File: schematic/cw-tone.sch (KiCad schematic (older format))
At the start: 20 parts, among them Q16 2N7000, Q17 2N7000, U10 NE5532

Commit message: Some minor tweaks
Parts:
- removed R62: 8.2K, symbol Device:R
- added RV6: 10K, symbol Device:R_POT_TRIM
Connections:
- net at D17.2 (A), D18.1 (K), R59.1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: now also RV6.1
- net at D17.1 (K), D18.2 (A), R55.1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: now also RV6.2, RV6.3
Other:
- note added: "Adjust to get a pure sine wave"
- moved on the sheet: C109, C112, Q17, R56, R57, R58, R60, R61

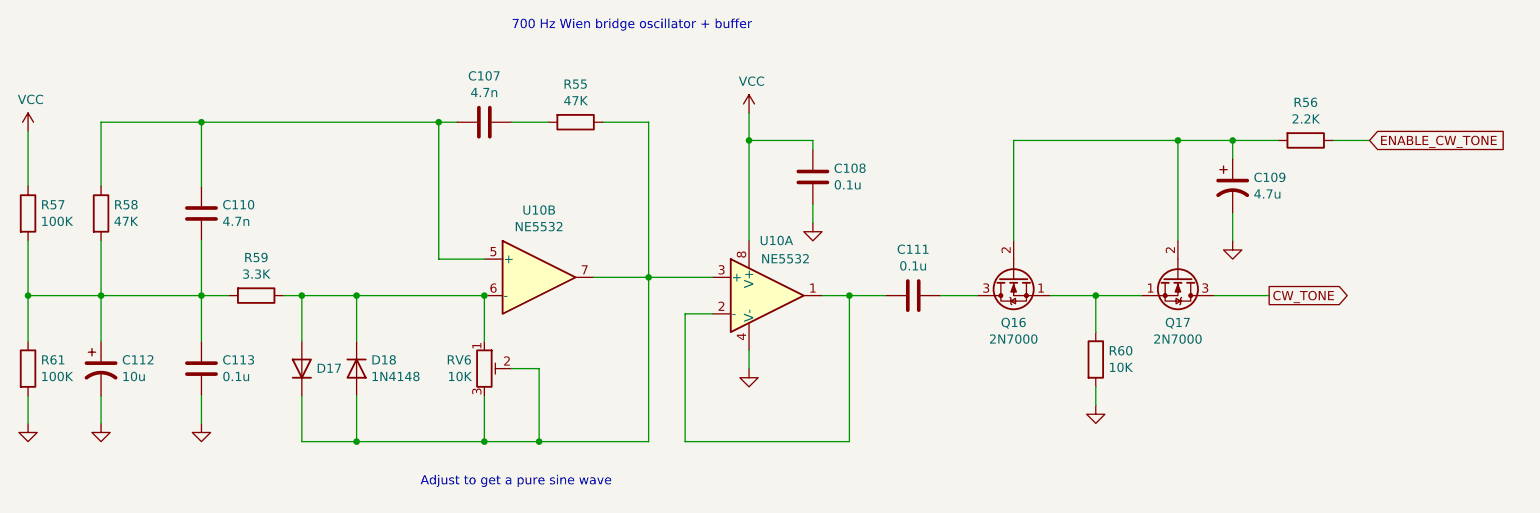
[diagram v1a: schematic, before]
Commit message: Correct the schematic
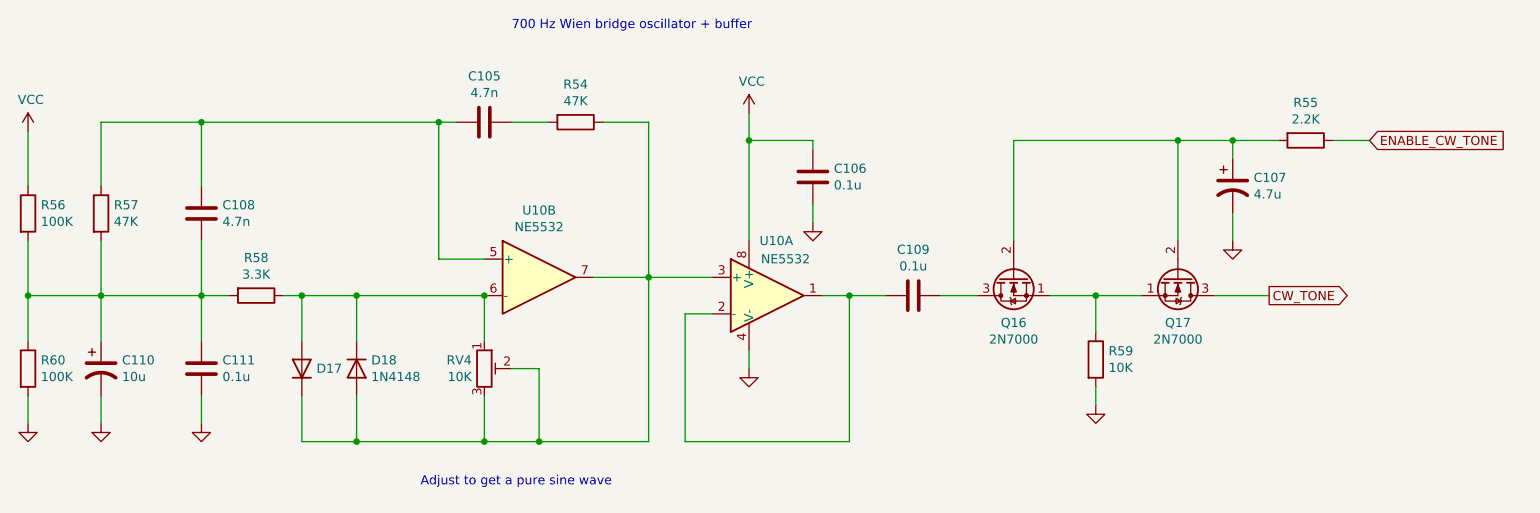
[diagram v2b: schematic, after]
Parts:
- renumbered C107 to C105, C108 to C106, C109 to C107, C110 to C108, C111 to C109, C112 to C110, C113 to C111, R55 to R54, R56 to R55, R57 to R56, R58 to R57, R59 to R58, R60 to R59, R61 to R60, RV6 to RV4
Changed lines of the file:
@@
 	5500 2450 5150 2450
 $Comp
-L power:GND #PWR0149
+L power:GND #PWR0148
 U 1 1 62E9F271
 P 5700 2950
-F 0 "#PWR0149" H 5700 2700 50  0001 C CNN
+F 0 "#PWR0148" H 5700 2700 50  0001 C CNN
 F 1 "GND" H 5705 2777 50  0001 C CNN
 F 2 "" H 5700 2950 50  0001 C CNN
@@
 	5700 2950 5700 2850
 $Comp
-L power:VCC #PWR0145
+L power:VCC #PWR0144
 U 1 1 62E9FFF5
 P 5700 1550
-F 0 "#PWR0145" H 5700 1400 50  0001 C CNN
+F 0 "#PWR0144" H 5700 1400 50  0001 C CNN
 F 1 "VCC" H 5715 1723 50  0000 C CNN
 F 2 "" H 5700 1550 50  0001 C CNN
@@
 $EndComp
 $Comp
-L Device:C C108
+L Device:C C106
 U 1 1 62EA0811
 P 6050 1900
-F 0 "C108" H 6165 1946 50  0000 L CNN
+F 0 "C106" H 6165 1946 50  0000 L CNN
 F 1 "0.1u" H 6165 1855 50  0000 L CNN
 F 2 "" H 6088 1750 50  0001 C CNN
@@
 $EndComp
 $Comp
-L power:GND #PWR0147
+L power:GND #PWR0146
 U 1 1 62EA1394
 P 6050 2150
-F 0 "#PWR0147" H 6050 1900 50  0001 C CNN
+F 0 "#PWR0146" H 6050 1900 50  0001 C CNN
 F 1 "GND" H 6055 1977 50  0001 C CNN
 F 2 "" H 6050 2150 50  0001 C CNN
@@
 Connection ~ 5700 1700
 $Comp
-L Device:C C111
+L Device:C C109
 U 1 1 62EA22EF
 P 6600 2550
-F 0 "C111" V 6348 2550 50  0000 C CNN
+F 0 "C109" V 6348 2550 50  0000 C CNN
 F 1 "0.1u" V 6439 2550 50  0000 C CNN
 F 2 "" H 6638 2400 50  0001 C CNN
@@
 Connection ~ 3550 3350
 $Comp
-L Device:R R59
+L Device:R R58
 U 1 1 62EAB701
 P 3000 2550
-F 0 "R59" V 2793 2550 50  0000 C CNN
+F 0 "R58" V 2793 2550 50  0000 C CNN
 F 1 "3.3K" V 2884 2550 50  0000 C CNN
 F 2 "" V 2930 2550 50  0001 C CNN
@@
 $EndComp
 $Comp
-L Device:C C113
+L Device:C C111
 U 1 1 62EB4018
 P 2700 2950
-F 0 "C113" H 2815 2996 50  0000 L CNN
+F 0 "C111" H 2815 2996 50  0000 L CNN
 F 1 "0.1u" H 2815 2905 50  0000 L CNN
 F 2 "" H 2738 2800 50  0001 C CNN
@@
 $EndComp
 $Comp
-L Device:CP1 C112
+L Device:CP1 C110
 U 1 1 62EB4E2D
 P 2150 2950
-F 0 "C112" H 2265 2996 50  0000 L CNN
+F 0 "C110" H 2265 2996 50  0000 L CNN
 F 1 "10u" H 2265 2905 50  0000 L CNN
 F 2 "" H 2150 2950 50  0001 C CNN
@@
 $EndComp
 $Comp
-L Device:R R61
+L Device:R R60
 U 1 1 62EB5CC9
 P 1750 2950
-F 0 "R61" H 1820 2996 50  0000 L CNN
+F 0 "R60" H 1820 2996 50  0000 L CNN
 F 1 "100K" H 1820 2905 50  0000 L CNN
 F 2 "" V 1680 2950 50  0001 C CNN
@@
 Connection ~ 3250 2550
 $Comp
-L power:GND #PWR0153
+L power:GND #PWR0152
 U 1 1 62EB7348
 P 2700 3250
-F 0 "#PWR0153" H 2700 3000 50  0001 C CNN
+F 0 "#PWR0152" H 2700 3000 50  0001 C CNN
 F 1 "GND" H 2705 3077 50  0001 C CNN
 F 2 "" H 2700 3250 50  0001 C CNN
@@
 $EndComp
 $Comp
-L power:GND #PWR0152
+L power:GND #PWR0151
 U 1 1 62EB7780
 P 2150 3250
-F 0 "#PWR0152" H 2150 3000 50  0001 C CNN
+F 0 "#PWR0151" H 2150 3000 50  0001 C CNN
 F 1 "GND" H 2155 3077 50  0001 C CNN
 F 2 "" H 2150 3250 50  0001 C CNN
@@
 $EndComp
 $Comp
-L power:GND #PWR0151
+L power:GND #PWR0150
 U 1 1 62EB79E4
 P 1750 3250
-F 0 "#PWR0151" H 1750 3000 50  0001 C CNN
+F 0 "#PWR0150" H 1750 3000 50  0001 C CNN
 F 1 "GND" H 1755 3077 50  0001 C CNN
 F 2 "" H 1750 3250 50  0001 C CNN
@@
 	2700 3100 2700 3250
 $Comp
-L Device:R R57
+L Device:R R56
 U 1 1 62EBA34E
 P 1750 2100
-F 0 "R57" H 1820 2146 50  0000 L CNN
+F 0 "R56" H 1820 2146 50  0000 L CNN
 F 1 "100K" H 1820 2055 50  0000 L CNN
 F 2 "" V 1680 2100 50  0001 C CNN
@@
 Connection ~ 1750 2550
 $Comp
-L power:VCC #PWR0146
+L power:VCC #PWR0145
 U 1 1 62EBB250
 P 1750 1650
-F 0 "#PWR0146" H 1750 1500 50  0001 C CNN
+F 0 "#PWR0145" H 1750 1500 50  0001 C CNN
 F 1 "VCC" H 1765 1823 50  0000 C CNN
 F 2 "" H 1750 1650 50  0001 C CNN
@@
 	1750 1950 1750 1650
 $Comp
-L Device:R R58
+L Device:R R57
 U 1 1 62EBC22D
 P 2150 2100
-F 0 "R58" H 2220 2146 50  0000 L CNN
+F 0 "R57" H 2220 2146 50  0000 L CNN
 F 1 "47K" H 2220 2055 50  0000 L CNN
 F 2 "" V 2080 2100 50  0001 C CNN
@@
 $EndComp
 $Comp
-L Device:C C110
+L Device:C C108
 U 1 1 62EBC657
 P 2700 2100
-F 0 "C110" H 2815 2146 50  0000 L CNN
+F 0 "C108" H 2815 2146 50  0000 L CNN
 F 1 "4.7n" H 2815 2055 50  0000 L CNN
 F 2 "" H 2738 1950 50  0001 C CNN
@@
 	2700 1600 4000 1600
 $Comp
-L Device:C C107
+L Device:C C105
 U 1 1 62EC01A5
 P 4250 1600
-F 0 "C107" V 3998 1600 50  0000 C CNN
+F 0 "C105" V 3998 1600 50  0000 C CNN
 F 1 "4.7n" V 4089 1600 50  0000 C CNN
 F 2 "" H 4288 1450 50  0001 C CNN
@@
 $EndComp
 $Comp
-L Device:R R55
+L Device:R R54
 U 1 1 62EC0F2F
 P 4750 1600
-F 0 "R55" V 4543 1600 50  0000 C CNN
+F 0 "R54" V 4543 1600 50  0000 C CNN
 F 1 "47K" V 4634 1600 50  0000 C CNN
 F 2 "" V 4680 1600 50  0001 C CNN
@@
 $EndComp
 $Comp
-L Device:R R60
+L Device:R R59
 U 1 1 62ECA784
 P 7600 2900
-F 0 "R60" H 7670 2946 50  0000 L CNN
+F 0 "R59" H 7670 2946 50  0000 L CNN
 F 1 "10K" H 7670 2855 50  0000 L CNN
 F 2 "" V 7530 2900 50  0001 C CNN
@@
 $EndComp
 $Comp
-L power:GND #PWR0150
+L power:GND #PWR0149
 U 1 1 62ECB46D
 P 7600 3150
-F 0 "#PWR0150" H 7600 2900 50  0001 C CNN
+F 0 "#PWR0149" H 7600 2900 50  0001 C CNN
 F 1 "GND" H 7605 2977 50  0001 C CNN
 F 2 "" H 7600 3150 50  0001 C CNN
@@
 	7150 1700 7150 2250
 $Comp
-L Device:CP1 C109
+L Device:CP1 C107
 U 1 1 62ED2ADC
 P 8350 1950
-F 0 "C109" H 8465 1996 50  0000 L CNN
+F 0 "C107" H 8465 1996 50  0000 L CNN
 F 1 "4.7u" H 8465 1905 50  0000 L CNN
 F 2 "" H 8350 1950 50  0001 C CNN
@@
 $EndComp
 $Comp
-L power:GND #PWR0148
+L power:GND #PWR0147
 U 1 1 62ED3541
 P 8350 2250
-F 0 "#PWR0148" H 8350 2000 50  0001 C CNN
+F 0 "#PWR0147" H 8350 2000 50  0001 C CNN
 F 1 "GND" H 8355 2077 50  0001 C CNN
 F 2 "" H 8350 2250 50  0001 C CNN
@@
 $EndComp
 $Comp
-L Device:R R56
+L Device:R R55
 U 1 1 62ED4001
 P 8750 1700
-F 0 "R56" V 8543 1700 50  0000 C CNN
+F 0 "R55" V 8543 1700 50  0000 C CNN
 F 1 "2.2K" V 8634 1700 50  0000 C CNN
 F 2 "" V 8680 1700 50  0001 C CNN
@@
 	7150 1700 8050 1700
 $Comp
-L Device:R_POT_TRIM RV6
+L Device:R_POT_TRIM RV4
 U 1 1 62FAD21E
 P 4250 2950
-F 0 "RV6" H 4181 2996 50  0000 R CNN
+F 0 "RV4" H 4181 2996 50  0000 R CNN
 F 1 "10K" H 4181 2905 50  0000 R CNN
 F 2 "" H 4250 2950 50  0001 C CNN
